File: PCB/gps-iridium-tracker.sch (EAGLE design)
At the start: 9 parts, among them J1 MICRO-USB, U1 ATMEGA32U4-XUMU

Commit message: Bit more
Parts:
- added C1, C4, C5: 4.7uF, SparkFun-Passives:CAP0603-CAP
- added C10, C11: 1uF, SparkFun-Passives:CAP0402-CAP
- added C12, C13, C14, C16, C17: 100nF, SparkFun-Passives:CAP0402-CAP
- added C2: 10uF, SparkFun-Passives:CAP0603-CAP
- added C20: 10nF, SparkFun-Passives:CAP0402-CAP
- added C21: 10uF, SparkFun-Passives:CAP0402-CAP
- added C3: 820pF, SparkFun-Passives:CAP0603-CAP
- added C6, C7: 1uF, SparkFun-Passives:CAP0603-CAP
- added C8, C9: 18pF, SparkFun-Passives:CAP0603-CAP
- added D1: B220A-13-F, !danielparts:B220A-13-F
- added JP1: Battery, SparkFun-Connectors:M02-JST-2MM-SMT
- added JP2: AVR-ISP-6, apex:AVR-ISP-6
- added L1: 3.3uH, bourns:INDUCTOR-SRN3015
- added LED1, LED4: RED, apex:LED
- added LED2: GREEN, apex:LED
- added LED3: YELLOW, apex:LED
- added R1: 30.1K, apex:R-EU_R0402
- added R10, R16, R17, R2, R3, R5, R7: 10K, apex:R-EU_R0402
- added R11, R12, R13, R6: 1K, apex:R-EU_R0402
- added R14: 7.5K, apex:R-EU_R0402
- added R15: 12K, apex:R-EU_R0402
- added R4: 120R, apex:R-EU_R0402
- added R8, R9: 22R, apex:R-EU_R0402
- added RESET: SPST_TACT-EVQQ2, adafruit:SPST_TACT-EVQQ2
- added U$5: STLM20, !danielparts:STLM20
- added U2: LMR62421, lmr62421:LMR62421_DBV_5
- added U3: MCP73831, SparkFun-PowerIC:MCP73831
- added U4: TLV70433, TLV704:TLV70433_DBV_5
- added Y1: (no value), !danielparts:CRYSTAL
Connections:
- removed net VCC: C18.1, C19.1, GPS.7_VCC_IO, GPS.8_VCC, GPS.9_V_RESET
- new net 3.3V: C10.2, C12.2, C13.2, C16.1, C17.2, C21.2, C7.1, JP2.2, R11.1, R12.1, R13.1, R7.2, U$3.VDD, U$3.VDD_IO, U$5.VCC, U1.AREF, U1.AVCC, U1.AVCC1, U1.UVCC, U1.VCC, U1.VCC1, U4.OUT
- new net 5V: C2.1, C3.2, D1.C, R1.2
- new net 5V_EN: R3.2, U2.EN
- new net BATT_READ: C14.1, R14.1, R15.2, U1.(ADC0)PF0
- new net CHG_STATUS: R4.2, R5.2, U3.STAT
- new net MISO: JP2.1, U1.(PD0/MISO/PCINT3)PB3
- new net MOSI: JP2.4, U1.(PDI/MOSI/PCINT2)PB2
- new net N$10: C11.2, U1.UCAP
- new net N$11: J1.2, R9.2
- new net N$12: J1.3, R8.2
- new net N$13: R10.2, U1.(#HWB)PE2
- new net N$14: C20.2, U$3.CAP
- new net N$15: LED4.A, R13.2
- new net N$16: LED2.A, R11.2
- new net N$17: LED3.A, R12.2
- new net N$18: R17.2, U$3.CS_A
- new net N$3: D1.A, L1.2, U2.SW
- new net N$4: C3.1, R1.1, R2.2, U2.FB
- new net N$5: LED1.C, R4.1
- new net N$6: R6.2, U3.PROG
- new net N$7: R16.2, U$3.CS_G
- new net N$8: C8.2, U1.XTAL2, Y1.2
- new net N$9: C9.2, U1.XTAL1, Y1.1
- new net RESET: JP2.5, R7.1, RESET.S, RESET.S1, U1.RESET
- new net RXLED: LED2.C, U1.(SS/PCINT0)PB0
- new net SCK: JP2.3, U1.(SCLK/PCINT1)PB1
- new net STATUSLED: LED4.C, U1.(ICP3/CLK0/OC4A)PC7
- new net TEMP: U$5.VOUT, U1.(ADC1)PF1
- new net TXLED: LED3.C, U1.(XCK1/#CTS)PD5
- new net USB_D+: R8.1, U1.D+
- new net USB_D-: R9.1, U1.D-
- new net VBAT: C1.2, C18.1, C19.1, C5.1, C6.2, GPS.7_VCC_IO, GPS.8_VCC, GPS.9_V_RESET, JP1.2, L1.1, R14.2, U2.VIN, U3.VBAT, U4.IN
- new net VUSB: C4.2, J1.1, LED1.A, R5.1, U1.VBUS, U3.VIN
- net GND: now also C1.1, C10.1, C11.1, C12.1, C13.1, C14.2, C16.2, C17.1, C2.2, C20.1, C21.1, C4.1, C5.2, C6.1, C7.2, C8.1, C9.1, J1.5, JP1.1, JP2.6, R10.1, R15.1, R16.1, R17.1, R2.1, R3.1, R6.1, RESET.P, RESET.P1, U$3.GND, U$5.GND, U1.GND, U1.GND1, U1.GND2, U1.GND3, U1.PAD, U1.UGND, U2.GND, U3.VSS, U4.GND
- net GPSRX: now also U1.(TXD1/INT3)PD3
- net GPSTX: now also U1.(RXD1/AIN1/INT2)PD2
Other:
- note added: "- Connect up LSM330DLC SPI - Connect up Iridium9603 - Add a flash chip"
- note added: "3.3V VReg"
- note added: "5V Boost Switching Reg"
- note added: "LiPo Charging Circuit"
- note added: "POWER"
- note added: "TODO"
- moved on the sheet: J1, U$2, U1

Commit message: Started PCB
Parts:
- removed U4: TLV70433, TLV704:TLV70433_DBV_5
- added C22, C23: 100nF, SparkFun-Passives:CAP0402-CAP
- added D2, D3: (no value), apex:DIODESOD
- added L2, L3: (no value), SparkFun-Passives:INDUCTOR0603
- added R18: 10K, apex:R-EU_R0402
- added SW1: CT10-XXXX-G1, switch-coto:CT10-XXXX-G1
- added U$7: TPS70933, !danielparts:TPS70933
- added U$8: FLASH, SparkFun-DigitalIC:SPI_FLASH-X25XXSMD
- C7: value 1uF -> 2.2uF
- JP1: device SparkFun-Connectors:M02-JST-2MM-SMT -> SparkFun-Connectors:M02JST-PTH-2
- JP2: value AVR-ISP-6 -> AVR-ISP-6SMD; device apex:AVR-ISP-6 -> apex:AVR-ISP-6SMD
- RESET: value SPST_TACT-EVQQ2 -> KMR441NGLFS; device adafruit:SPST_TACT-EVQQ2 -> apex:KMR441NGLFS
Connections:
- removed net N$2: C15.1, U$1.FEED
- removed net N$7: R16.2, U$3.CS_G
- new net 3.3V_EN: D2.C, D3.C, R17.2, U$7.EN
- new net CS_A: U$3.CS_A, U1.(PCINT7/OC0A/OC1C/#RTS)PB7
- new net CS_F: U$8.CS
- new net CS_G: U$3.CS_G, U1.(INT6/AIN0)PE6
- new net KEEPON: D3.A, U1.(SDA/INT1)PD1
- new net ON: R18.2, U1.(OC0B/SCL/INT0)PD0
- new net SAT_AVAIL: U$2.NET_AVAIL, U1.(PCINT5/OC1A/#OC4B/ADC12)PB5
- new net SAT_EN: R16.1, U$2.ON/OFF, U1.(ICP1/ADC8)PD4
- new net SAT_RI: U$2.DF_RI, U1.(ADC11/PCINT4)PB4
- new net SAT_RX: U$2.DF_S_RX, U1.(T0/OC4D/ADC10)PD7
- new net SAT_TX: U$2.DF_S_TX, U1.(T1/#OC4D/ADC9)PD6
- net 3.3V: now also C18.1, C19.1, C23.1, GPS.7_VCC_IO, GPS.8_VCC, GPS.9_V_RESET, U$7.VOUT, U$8.VCC; no longer U4.OUT
- net 5V: now also C22.1, U$2.EXT_PWR
- net GND: now also C22.2, C23.2, R16.2, U$2.EXT_GND, U$2.SIG_GND, U$7.GND, U$8.GND; no longer R16.1, U4.GND
- net MISO: now also U$3.SDO_A, U$3.SDO_G, U$8.MISO
- net MOSI: now also U$3.SDA_A/G, U$8.MOSI
- net N$1: now also U$1.FEED; no longer C15.2
- net N$18: now also D2.A, R18.1, SW1.2; no longer R17.2, U$3.CS_A
- net SCK: now also U$3.SCL_A/G, U$8.SCK
- net VBAT: now also SW1.1, U$7.VIN; no longer C18.1, C19.1, GPS.7_VCC_IO, GPS.8_VCC, GPS.9_V_RESET, U4.IN
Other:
- note added: "Reed Switch"
- note removed: "- Connect up LSM330DLC SPI - Connect up Iridium9603 - Add a flash chip"
- note removed: "TODO"
- moved on the sheet: C1, C15, C16, C17, C18, C19, C2, C20, C21, C3, C6, C7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

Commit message: PCB
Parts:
- Y1: value (none) -> 8Z; device !danielparts:CRYSTAL -> !danielparts:8Z
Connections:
- net GND: now also Y1.GND
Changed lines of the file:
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@@
 <part name="R7" library="apex" deviceset="R-EU_" device="R0402" value="10K"/>
 <part name="P+6" library="apex" deviceset="3.3V" device=""/>
-<part name="Y1" library="!danielparts" deviceset="CRYSTAL" device=""/>
+<part name="Y1" library="!danielparts" deviceset="8Z" device=""/>
 <part name="C8" library="SparkFun-Passives" deviceset="CAP" device="0603-CAP" value="18pF"/>
 <part name="C9" library="SparkFun-Passives" deviceset="CAP" device="0603-CAP" value="18pF"/>
@@
 <wire x1="345.44" y1="55.88" x2="342.9" y2="55.88" width="0.1524" layer="91"/>
 </segment>
+<segment>
+<pinref part="Y1" gate="G$1" pin="GND"/>
+<wire x1="233.68" y1="213.36" x2="236.22" y2="213.36" width="0.1524" layer="91"/>
+</segment>
 </net>

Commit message: Finished PCB
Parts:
- removed C15: 1pF, apex:CAP0402-CAP
- removed L2, L3: (no value), SparkFun-Passives:INDUCTOR0603
- U1: value ATMEGA32U4-XUMU -> SMARTPRJ_ATMEGA32U4-XUMU; device SmartPrj:ATMEGA32U4-XUMU -> gps-iridium-tracker:SMARTPRJ_ATMEGA32U4-XUMU
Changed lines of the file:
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@@
 <part name="FRAME1" library="apex" deviceset="FRAME-A3" device=""/>
 <part name="U$1" library="Ava" deviceset="JTI_ANTENNA-1575AT54A0010" device=""/>
-<part name="C15" library="apex" deviceset="CAP" device="0402-CAP" value="1pF"/>
-<part name="U1" library="SmartPrj" deviceset="ATMEGA32U4-XU" device="MU"/>
+<part name="U1" library="gps-iridium-tracker" deviceset="SMARTPRJ_ATMEGA32U4-XU" device="MU"/>
 <part name="U$2" library="!danielparts" deviceset="IRIDIUM9603" device=""/>
 <part name="U$3" library="LSM330DLC" deviceset="LSM330DLC" device=""/>
@@
 <part name="C23" library="SparkFun-Passives" deviceset="CAP" device="0402-CAP" value="100nF"/>
 <part name="GND36" library="apex" deviceset="GND" device=""/>
-<part name="L2" library="SparkFun-Passives" deviceset="INDUCTOR" device="0603"/>
-<part name="L3" library="SparkFun-Passives" deviceset="INDUCTOR" device="0603"/>
 <part name="P+9" library="apex" deviceset="3.3V" device=""/>
 </parts>
@@
 <instance part="FRAME1" gate="G$1" x="0" y="0"/>
 <instance part="U$1" gate="G$1" x="30.48" y="66.04" rot="MR180"/>
-<instance part="C15" gate="G$1" x="63.5" y="30.48" smashed="yes" rot="MR270">
-<attribute name="NAME" x="61.214" y="28.321" size="1.778" layer="95" rot="MR0"/>
-<attribute name="VALUE" x="68.961" y="28.194" size="1.778" layer="96" rot="MR0"/>
-</instance>
 <instance part="U1" gate="G$1" x="261.62" y="205.74"/>
 <instance part="U$2" gate="G$1" x="213.36" y="48.26"/>
@@
 </instance>
 <instance part="GND36" gate="1" x="347.98" y="55.88" rot="R90"/>
-<instance part="L2" gate="G$1" x="43.18" y="35.56"/>
-<instance part="L3" gate="G$1" x="53.34" y="35.56"/>
 <instance part="P+9" gate="G$1" x="124.46" y="71.12"/>
 </instances>

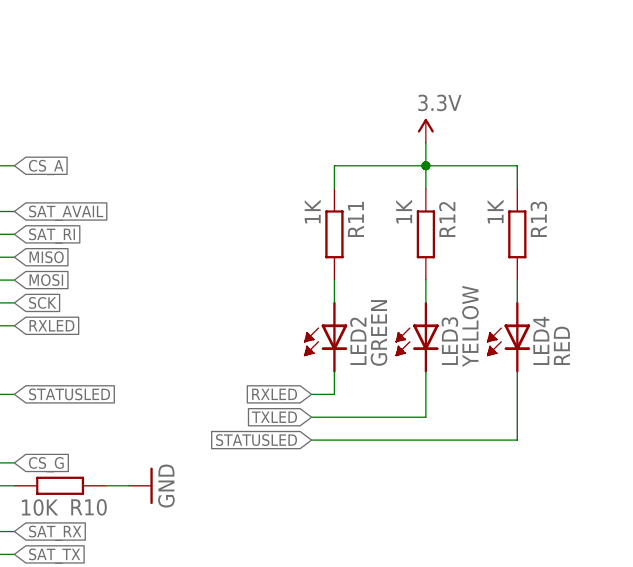
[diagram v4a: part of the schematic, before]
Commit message: Changed led resistor values
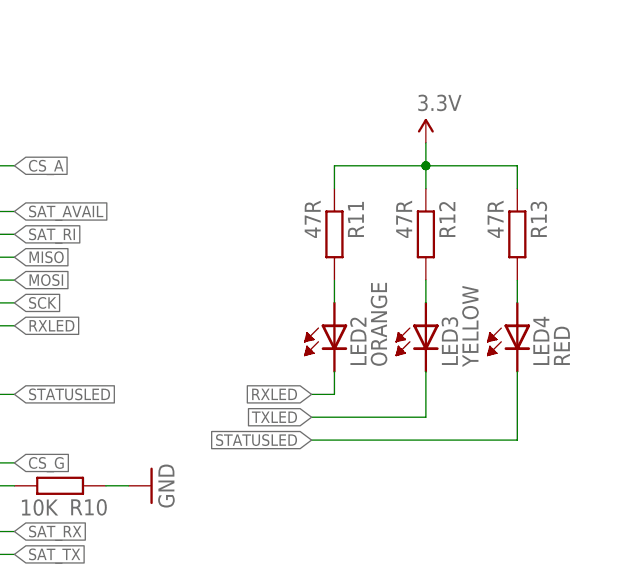
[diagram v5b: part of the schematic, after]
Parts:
- LED2: value GREEN -> ORANGE
- R11, R12, R13: value 1K -> 47R
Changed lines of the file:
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@@
 <?xml version="1.0" encoding="utf-8"?>
 <!DOCTYPE eagle SYSTEM "eagle.dtd">
-<eagle version="6.3">
+<eagle version="6.4">
 <drawing>
 <settings>
@@
 <part name="R10" library="apex" deviceset="R-EU_" device="R0402" value="10K"/>
 <part name="GND24" library="apex" deviceset="GND" device=""/>
-<part name="LED2" library="apex" deviceset="LED" device="" value="GREEN"/>
+<part name="LED2" library="apex" deviceset="LED" device="" value="ORANGE"/>
 <part name="LED3" library="apex" deviceset="LED" device="" value="YELLOW"/>
-<part name="R11" library="apex" deviceset="R-EU_" device="R0402" value="1K"/>
-<part name="R12" library="apex" deviceset="R-EU_" device="R0402" value="1K"/>
+<part name="R11" library="apex" deviceset="R-EU_" device="R0402" value="47R"/>
+<part name="R12" library="apex" deviceset="R-EU_" device="R0402" value="47R"/>
 <part name="P+11" library="apex" deviceset="3.3V" device=""/>
-<part name="R13" library="apex" deviceset="R-EU_" device="R0402" value="1K"/>
+<part name="R13" library="apex" deviceset="R-EU_" device="R0402" value="47R"/>
 <part name="LED4" library="apex" deviceset="LED" device="" value="RED"/>
 <part name="JP2" library="apex" deviceset="AVR-ISP-6" device="SMD" value="AVR-ISP-6SMD"/>
